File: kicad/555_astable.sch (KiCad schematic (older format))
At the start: 10 parts, among them U2 555

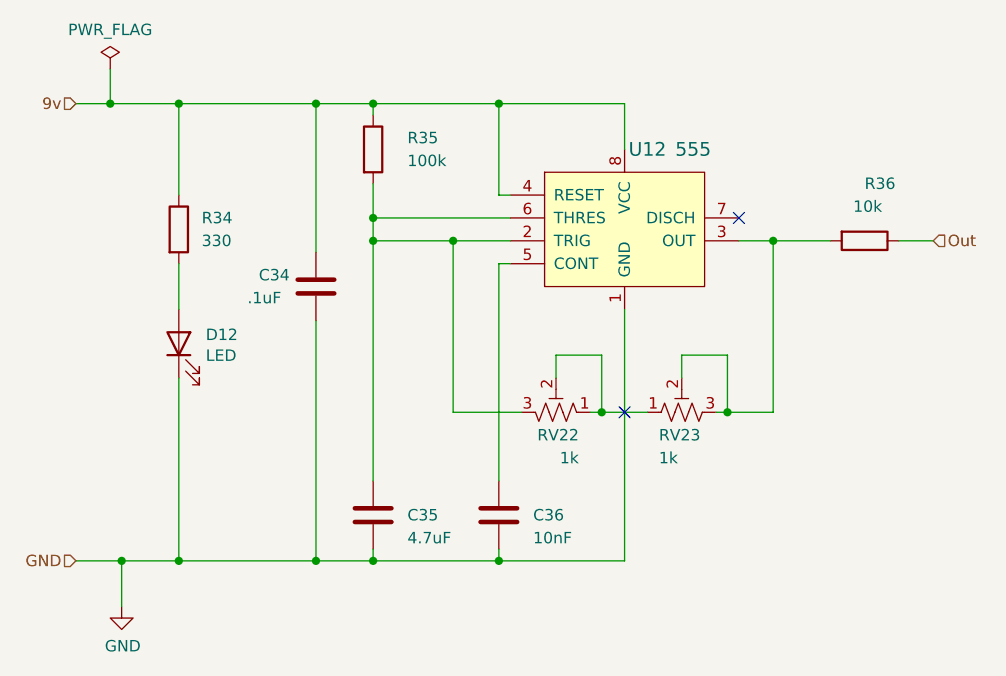
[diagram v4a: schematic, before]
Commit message: Re-annotate and update footprints
* vertical resistors
* radial, electrolytics timing caps
* add switch
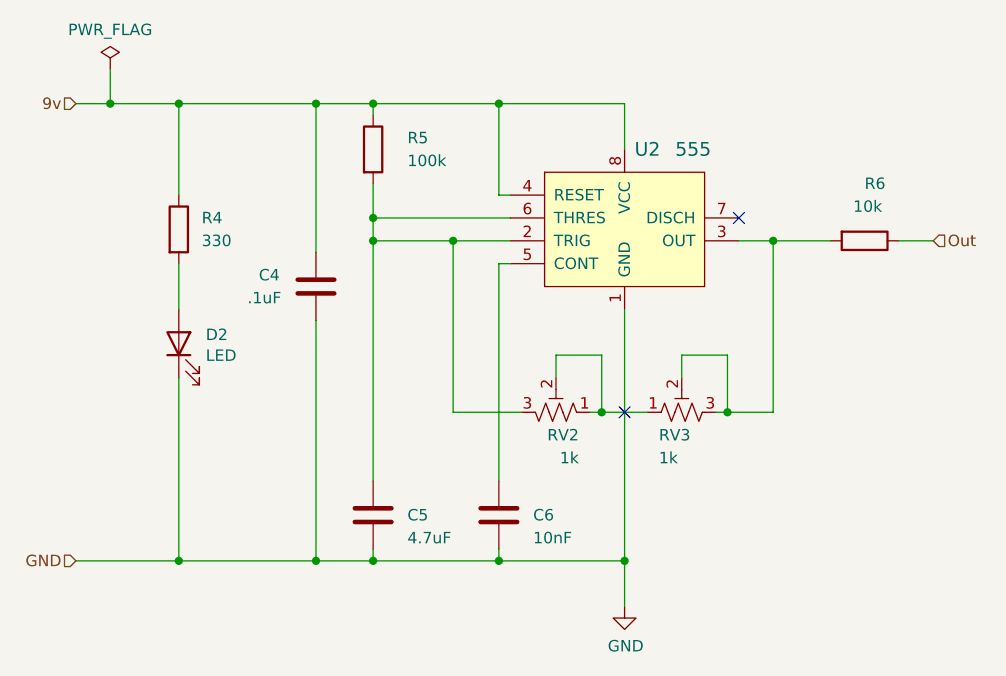
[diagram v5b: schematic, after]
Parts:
- C5: footprint Capacitor_THT:C_Disc_D5.0mm_W2.5mm_P5.00mm -> Capacitor_THT:CP_Radial_D4.0mm_P2.00mm
- R5, R6: footprint Resistor_THT:R_Axial_DIN0204_L3.6mm_D1.6mm_P7.62mm_Horizontal -> Resistor_THT:R_Axial_DIN0207_L6.3mm_D2.5mm_P2.54mm_Vertical

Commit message: Swap pot footprint
Still not the correct component that I'm using, but this one at least
has larger holes for its legs (instead of wire leads) which I'm hoping
will make the pots easier to insert
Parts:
- RV3: footprint Potentiometer_THT:Potentiometer_Bourns_3386F_Vertical -> Potentiometer_THT:Potentiometer_Piher_PT-6-V_Vertical
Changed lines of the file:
@@
 F 0 "RV3" V 5850 4700 50  0000 R CNN
 F 1 "1k" V 5750 4700 50  0000 R CNN
-F 2 "Potentiometer_THT:Potentiometer_Bourns_3386F_Vertical" H 5950 4600 50  0001 C CNN
+F 2 "Potentiometer_THT:Potentiometer_Piher_PT-6-V_Vertical" H 5950 4600 50  0001 C CNN
 F 3 "~" H 5950 4600 50  0001 C CNN
 F 4 "Course" V 5950 4600 50  0001 C CNN "Description"

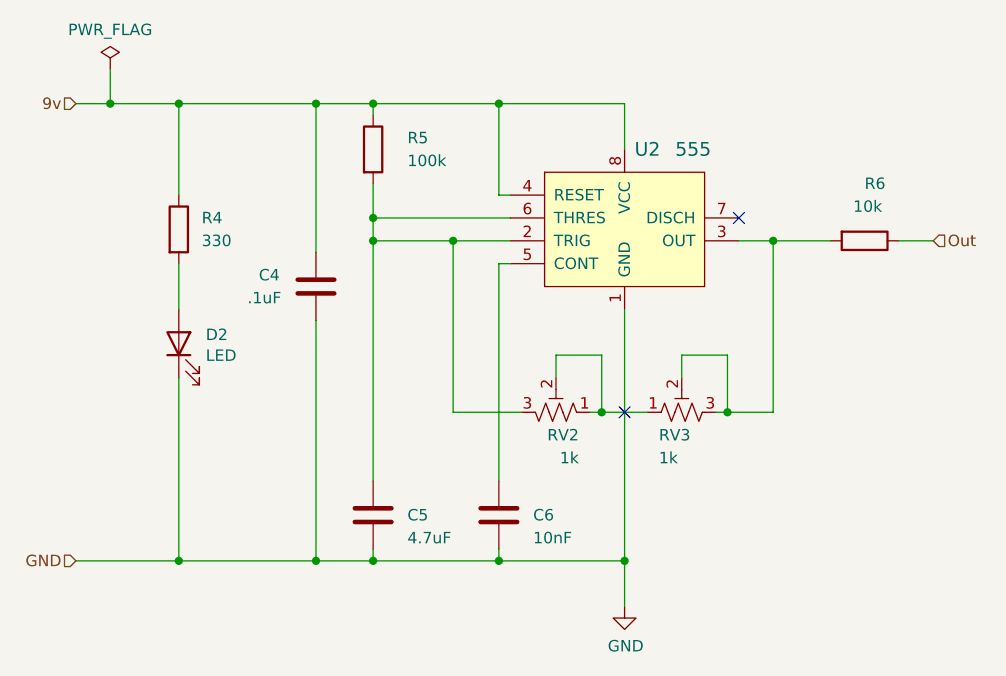
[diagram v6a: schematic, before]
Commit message: Re-annotate to fix key vs 555 mismatch
The alignment of switch to 555 circuit was off, starting around S8. I
believe this was from non-linear copy-pasting when key count jumped from
13 to 20.

No amound of fiddling with the annotation tool seemed to fix and to do
it manually was out of the question, so I ended up deleting 6-20 and
copy-pasting 1-5 three times. I think it worked...
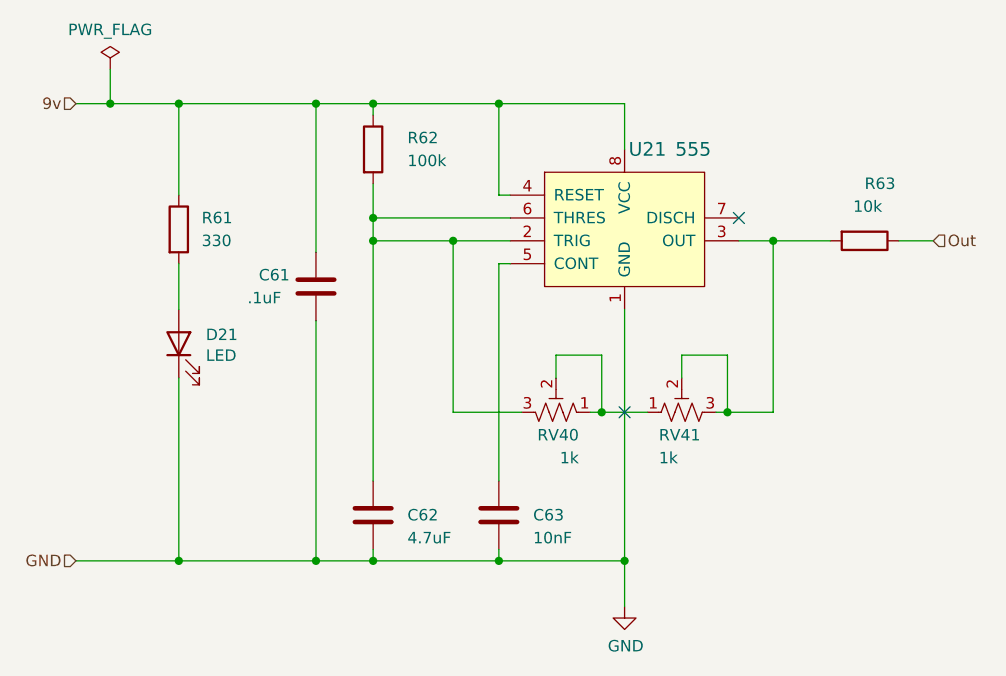
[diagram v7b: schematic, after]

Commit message: Start new PCB layout
* wider cavity w/o top
* swap fine trimmer for resistor
* bigger wire holes for speaker,battery
* 5mm LEDs
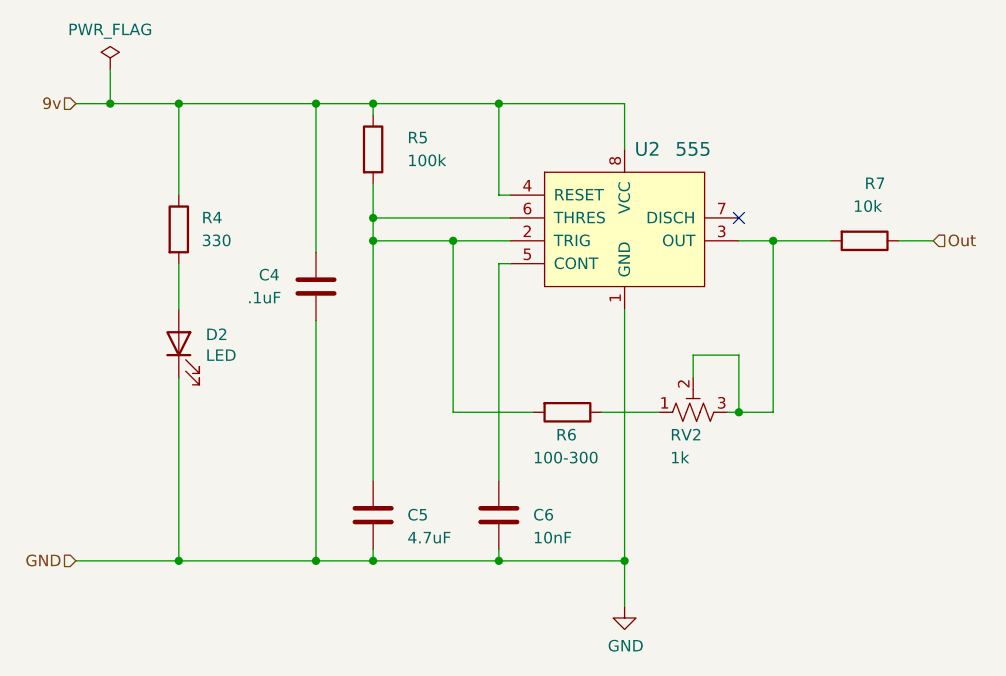
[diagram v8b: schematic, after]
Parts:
- removed RV2: 1k, Potentiometer_THT:Potentiometer_Bourns_3296W_Vertical, symbol Device:R_POT_TRIM_US
- added R6: 100-300, Resistor_THT:R_Axial_DIN0207_L6.3mm_D2.5mm_P2.54mm_Vertical, symbol Device:R
- D2: footprint LED_THT:LED_D3.0mm -> LED_THT:LED_D5.0mm
- renumbered R6 to R7, RV3 to RV2
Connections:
- net at RV2.1: now also R6.1
- net at C5.1, R5.2, U2.2 (TRIG)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: now also R6.2
- no-connect marks 2 -> 1
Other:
- moved on the sheet: RV2
